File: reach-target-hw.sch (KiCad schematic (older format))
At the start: 29 parts, among them U1 nRF51822-QF, X1 16MHz 40ppm, X2 32.768kHz 20ppm

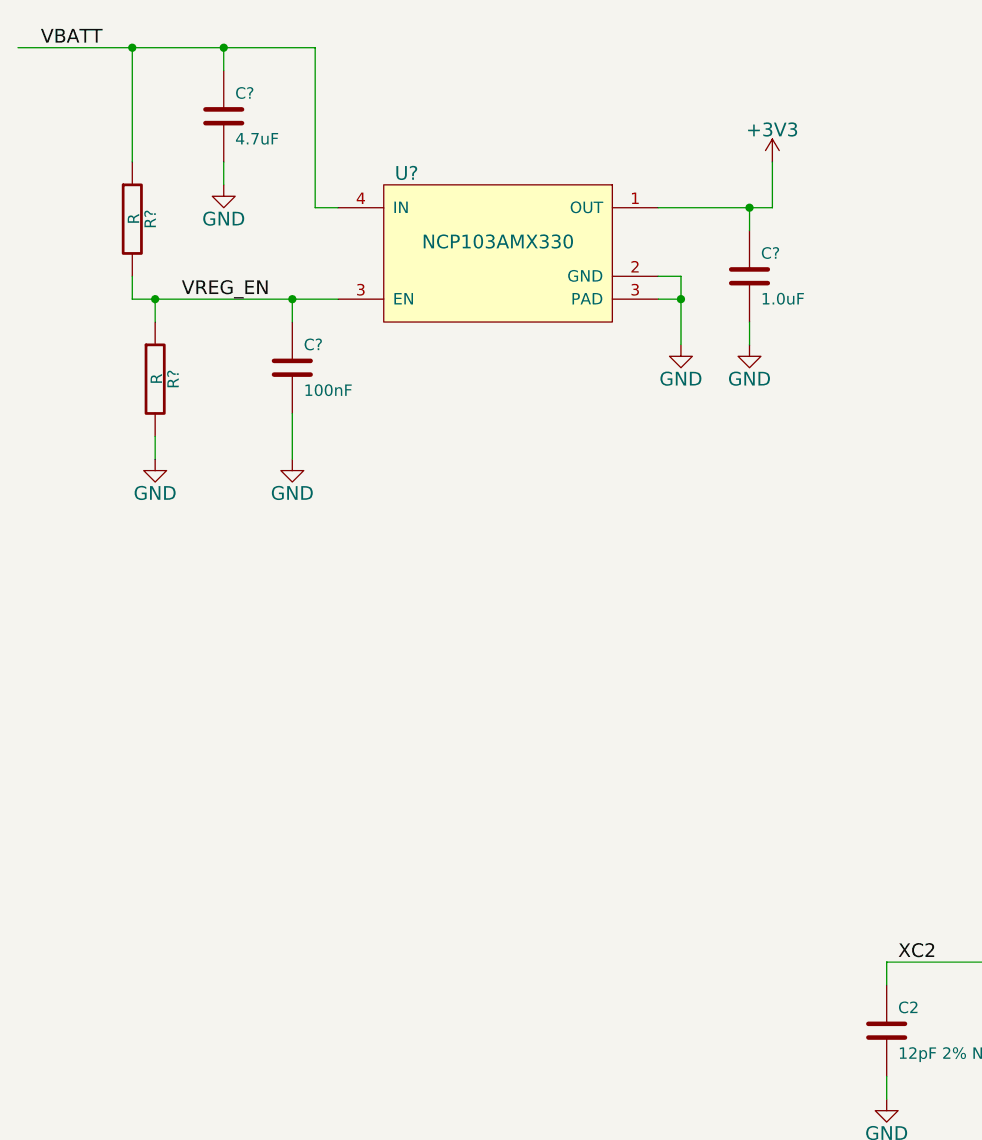
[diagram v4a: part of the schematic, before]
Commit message: added eeprom. can be no-popped
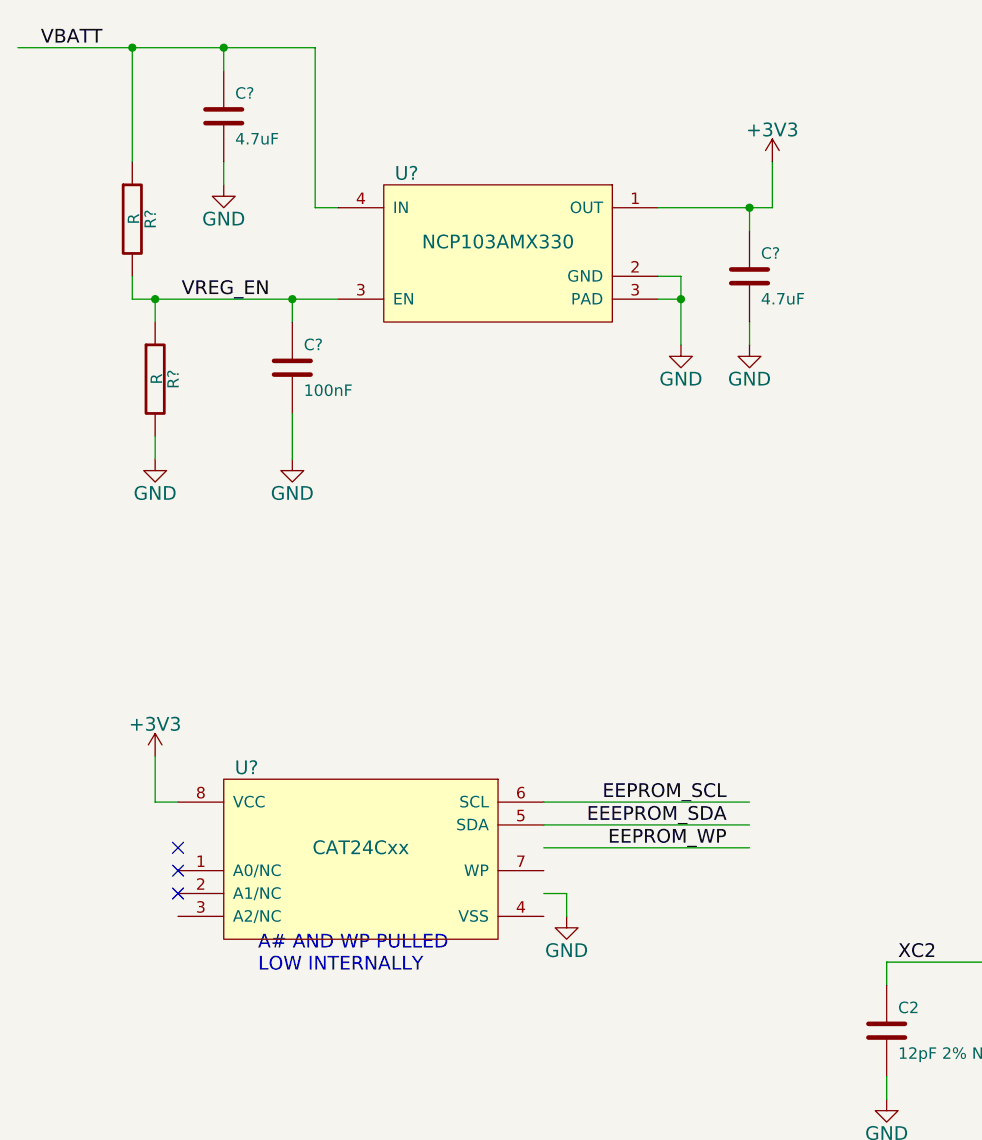
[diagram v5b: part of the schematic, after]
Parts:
- added U?: CAT24Cxx, symbol CAT24Cxx
- C?: value 1.0uF -> 4.7uF
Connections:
- net labels added: EEEPROM_SDA, EEPROM_SCL, EEPROM_WP
- wire segments 108 -> 115
- no-connect marks 1 -> 4
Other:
- note added: "A# AND WP PULLED\nLOW INTERNALLY"

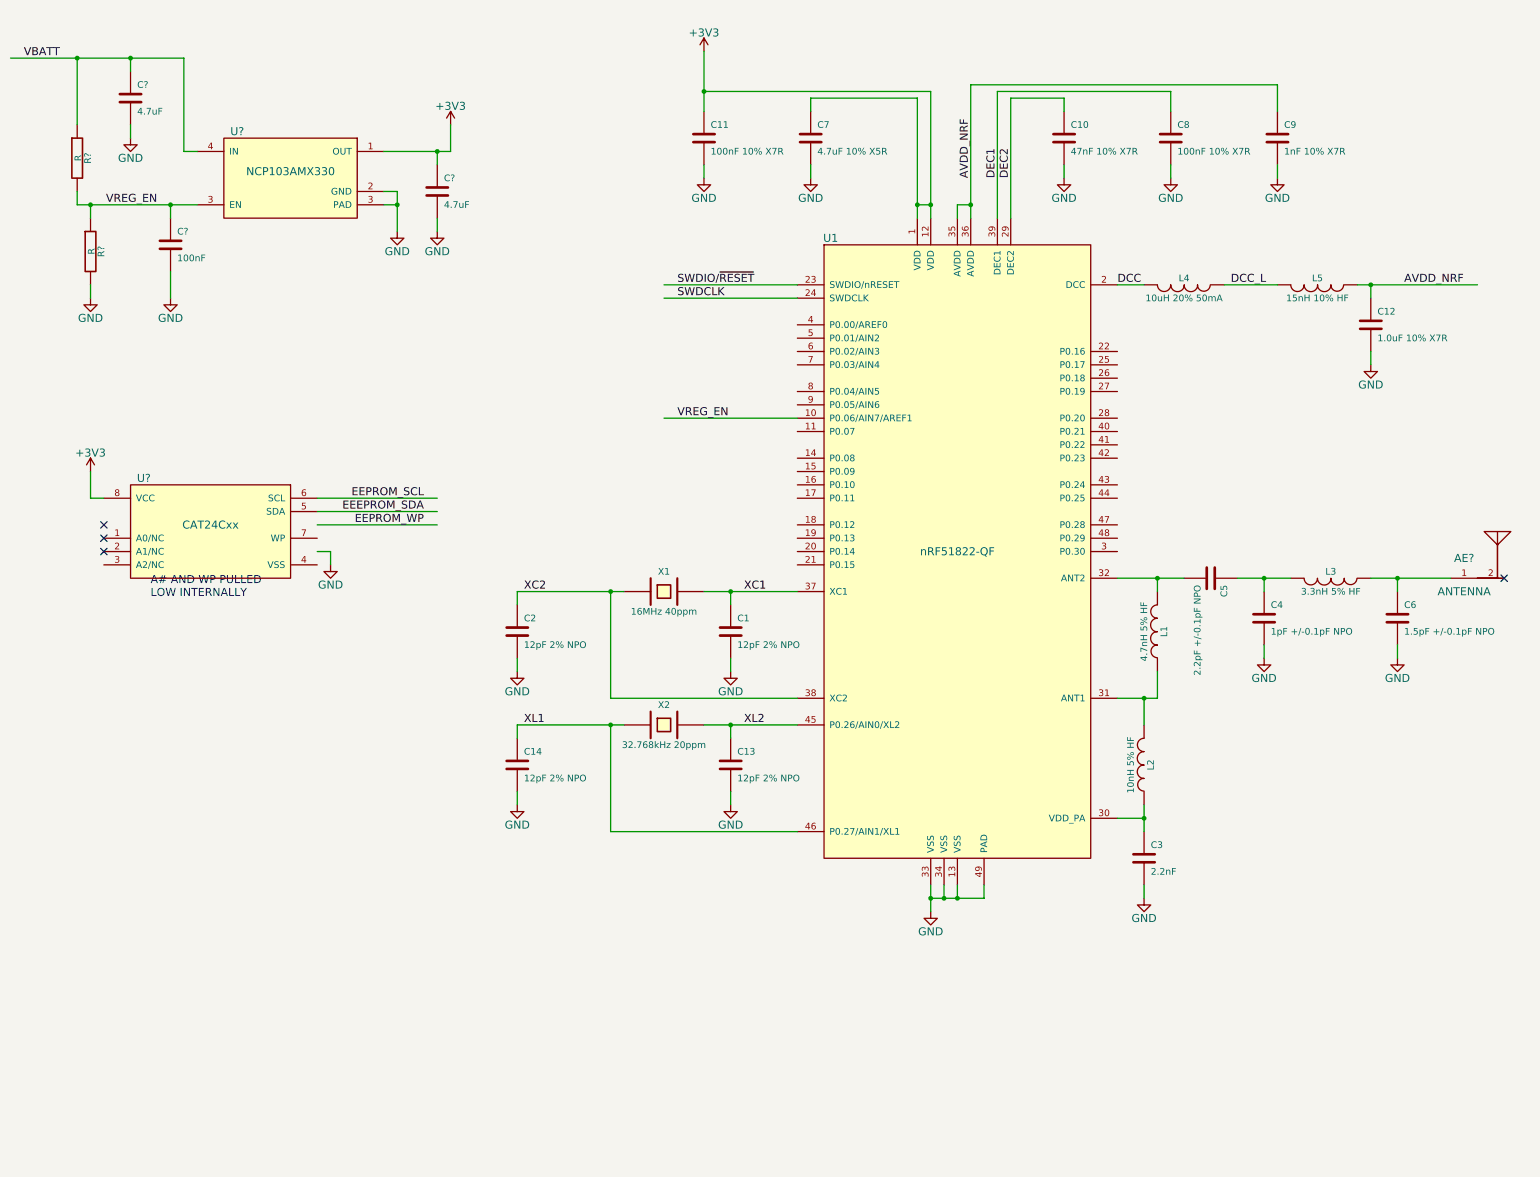
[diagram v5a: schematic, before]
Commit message: connected eeprom wp
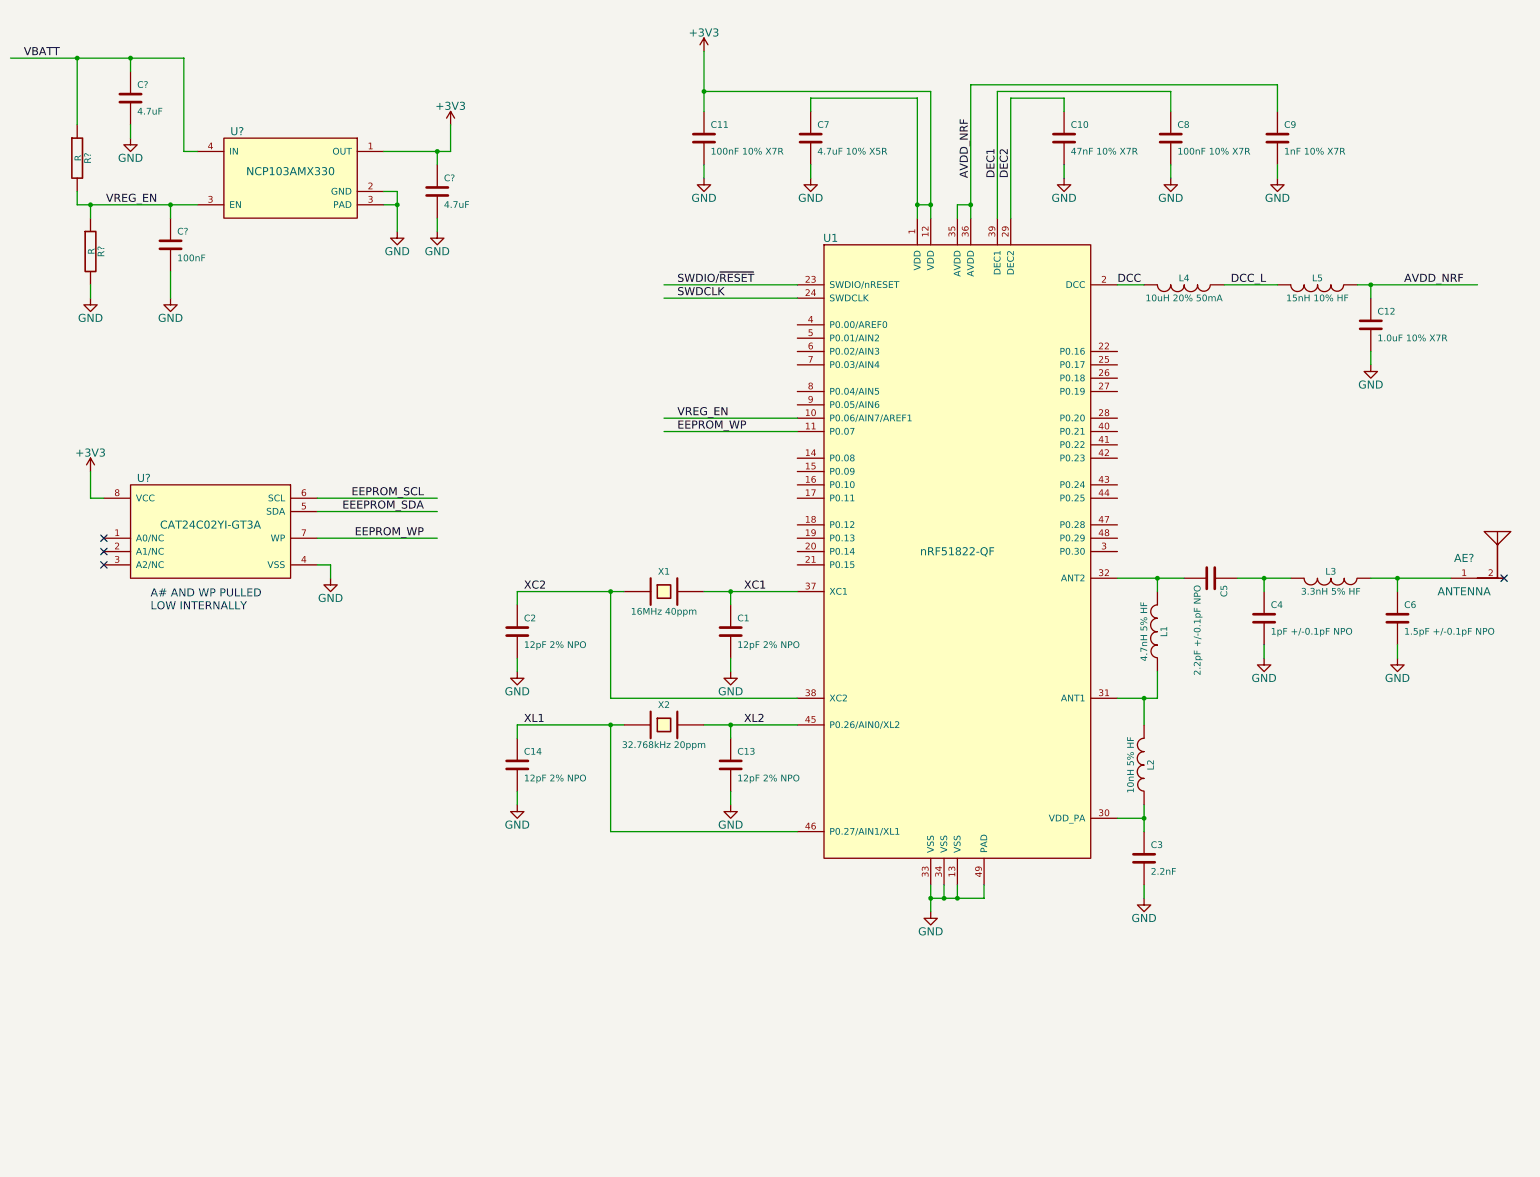
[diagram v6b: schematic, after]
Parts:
- U?: value CAT24Cxx -> CAT24C02YI-GT3A; footprint (none) -> Housings_SSOP:TSSOP-8_3x3mm_Pitch0.65mm
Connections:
- wire segments 115 -> 93
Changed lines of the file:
@@
 P 2800 5200
 F 0 "U?" H 2300 5550 60  0000 C CNN
-F 1 "CAT24Cxx" H 2800 5200 60  0000 C CNN
-F 2 "" H 2800 5200 60  0000 C CNN
-F 3 "" H 2800 5200 60  0000 C CNN
+F 1 "CAT24C02YI-GT3A" H 2800 5200 60  0000 C CNN
+F 2 "Housings_SSOP:TSSOP-8_3x3mm_Pitch0.65mm" H 2800 5200 60  0001 C CNN
+F 3 "http://www.onsemi.com/pub_link/Collateral/CAT24C01-D.PDF" H 2800 5200 60  0001 C CNN
 	1    2800 5200
 	1    0    0    -1
@@
 L GND #PWR?
 U 1 1 54D4057E
-P 3700 5500
-F 0 "#PWR?" H 3700 5250 60  0001 C CNN
-F 1 "GND" H 3700 5350 60  0000 C CNN
-F 2 "" H 3700 5500 60  0000 C CNN
-F 3 "" H 3700 5500 60  0000 C CNN
-	1    3700 5500
+P 3700 5600
+F 0 "#PWR?" H 3700 5350 60  0001 C CNN
+F 1 "GND" H 3700 5450 60  0000 C CNN
+F 2 "" H 3700 5600 60  0000 C CNN
+F 3 "" H 3700 5600 60  0000 C CNN
+	1    3700 5600
 	1    0    0    -1
 $EndComp
@@
 	1900 5000 1900 4800
 Wire Wire Line
-	3700 5400 3600 5400
-Wire Wire Line
-	3700 5500 3700 5400
+	3700 5500 3600 5500
+Wire Wire Line
+	3700 5600 3700 5500
 Wire Wire Line
 	6200 4400 7200 4400
@@
 Connection ~ 2500 2800
 Wire Wire Line
-	2500 2900 2500 2800
-Wire Wire Line
-	1800 2800 1900 2800
-Wire Wire Line
-	1900 2800 2500 2800
-Wire Wire Line
-	2500 2800 2700 2800
+	2500 2800 2500 2900
+Wire Wire Line
+	1800 2800 2700 2800
 Wire Wire Line
 	2200 2300 2200 2200
@@
 	2200 1700 2200 1800
 Wire Wire Line
-	1300 1700 1800 1700
-Wire Wire Line
-	1800 1700 2200 1700
-Wire Wire Line
-	2200 1700 2600 1700
+	1300 1700 2600 1700
 Wire Wire Line
 	2600 2400 2700 2400
@@
 	4200 2800 4100 2800
 Wire Wire Line
-	4200 2700 4200 2800
-Wire Wire Line
-	4200 2800 4200 3000
+	4200 2700 4200 3000
 Wire Wire Line
 	4100 2700 4200 2700
 Wire Wire Line
-	4100 2400 4500 2400
-Wire Wire Line
-	4500 2400 4600 2400
+	4100 2400 4600 2400
 Wire Wire Line
 	4600 2400 4600 2200
@@
 	11700 5600 11700 5700
 Wire Wire Line
-	11500 5600 11700 5600
-Wire Wire Line
-	11700 5600 12100 5600
+	11500 5600 12100 5600
 Connection ~ 10700 5600
 Wire Wire Line
@@
 	10700 5600 10700 5700
 Wire Wire Line
-	10500 5600 10700 5600
-Wire Wire Line
-	10700 5600 10900 5600
+	10500 5600 10900 5600
 Connection ~ 9900 5600
 Connection ~ 9800 7400
@@
 	9900 5600 9900 5700
 Wire Wire Line
-	9600 5600 9900 5600
-Wire Wire Line
-	9900 5600 10100 5600
-Wire Wire Line
-	9800 7300 9800 7400
-Wire Wire Line
-	9800 7400 9800 7500
+	9600 5600 10100 5600
+Wire Wire Line
+	9800 7300 9800 7500
 Wire Wire Line
 	9600 7400 9800 7400
@@
 	9900 6500 9900 6300
 Wire Wire Line
-	9600 6500 9800 6500
-Wire Wire Line
-	9800 6500 9900 6500
+	9600 6500 9900 6500
 Connection ~ 8500 2800
 Wire Wire Line
@@
 	8500 2800 8400 2800
 Wire Wire Line
-	8500 1900 8500 2800
-Wire Wire Line
-	8500 2800 8500 2900
+	8500 1900 8500 2900
 Wire Wire Line
 	10800 1900 10800 2100
@@
 	11500 3400 11500 3500
 Wire Wire Line
-	11400 3400 11500 3400
-Wire Wire Line
-	11500 3400 12300 3400
+	11400 3400 12300 3400
 Wire Wire Line
 	10400 3400 10800 3400
@@
 	5100 6700 5100 6800
 Wire Wire Line
-	5100 6700 5800 6700
-Wire Wire Line
-	5800 6700 5900 6700
+	5100 6700 5900 6700
 Wire Wire Line
 	5800 7500 5800 6700
@@
 	6700 7300 6700 7200
 Wire Wire Line
-	6500 6700 6700 6700
-Wire Wire Line
-	6700 6700 7200 6700
+	6500 6700 7200 6700
 Wire Wire Line
 	5100 6300 5100 6200
@@
 	5100 5700 5100 5800
 Wire Wire Line
-	5100 5700 5800 5700
-Wire Wire Line
-	5800 5700 5900 5700
+	5100 5700 5900 5700
 Wire Wire Line
 	5800 6500 5800 5700
@@
 	6700 6300 6700 6200
 Wire Wire Line
-	6500 5700 6700 5700
-Wire Wire Line
-	6700 5700 7200 5700
+	6500 5700 7200 5700
 Connection ~ 8100 2800
 Connection ~ 8200 2800
@@
 	8100 2800 8200 2800
 Wire Wire Line
-	8200 1950 8200 2800
-Wire Wire Line
-	8200 2800 8200 2900
+	8200 1950 8200 2900
 Wire Wire Line
 	6500 1950 8200 1950
 Wire Wire Line
-	6500 1650 6500 1950
-Wire Wire Line
-	6500 1950 6500 2100
+	6500 1650 6500 2100
 Wire Wire Line
 	6500 2600 6500 2500
@@
 	8100 2000 7300 2000
 Wire Wire Line
-	8100 2000 8100 2800
-Wire Wire Line
-	8100 2800 8100 2900
+	8100 2000 8100 2900
 Wire Wire Line
 	7300 2600 7300 2500
@@
 Connection ~ 8200 8000
 Wire Wire Line
-	8200 8000 8300 8000
-Wire Wire Line
-	8300 8000 8400 8000
-Wire Wire Line
-	8400 8000 8600 8000
+	8200 8000 8600 8000
 Wire Wire Line
 	8300 7900 8300 8000
 Wire Wire Line
-	8200 7900 8200 8000
-Wire Wire Line
-	8200 8000 8200 8100
-NoConn ~ 2000 5200
+	8200 7900 8200 8100
+NoConn ~ 2000 5500
 NoConn ~ 2000 5300
 NoConn ~ 2000 5400
@@
 Wire Wire Line
 	4500 5100 3600 5100
-Text Notes 2350 5750 0    60   ~ 0
+Text Notes 2350 5850 0    60   ~ 0
 A# AND WP PULLED\nLOW INTERNALLY
 Wire Wire Line
-	4500 5200 3600 5200
-Text Label 4400 5200 2    60   ~ 0
+	4500 5300 3600 5300
+Text Label 4400 5300 2    60   ~ 0
 EEPROM_WP
 Text Label 4400 5100 2    60   ~ 0
@@
 Text Label 4400 5000 2    60   ~ 0
 EEPROM_SCL
+Text Label 6300 4500 0    60   ~ 0
+EEPROM_WP
+Wire Wire Line
+	6200 4500 7200 4500
 $EndSCHEMATC

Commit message: labels
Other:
- note added: "3.3V LDO"
- note added: "I2C EEPROM"
- moved on the sheet: U?
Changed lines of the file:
@@
 L CAT24Cxx U?
 U 1 1 54D4022B
-P 2800 5200
-F 0 "U?" H 2300 5550 60  0000 C CNN
-F 1 "CAT24C02YI-GT3A" H 2800 5200 60  0000 C CNN
-F 2 "Housings_SSOP:TSSOP-8_3x3mm_Pitch0.65mm" H 2800 5200 60  0001 C CNN
-F 3 "http://www.onsemi.com/pub_link/Collateral/CAT24C01-D.PDF" H 2800 5200 60  0001 C CNN
-	1    2800 5200
+P 2400 5400
+F 0 "U?" H 1900 5750 60  0000 C CNN
+F 1 "CAT24C02YI-GT3A" H 2400 5400 60  0000 C CNN
+F 2 "Housings_SSOP:TSSOP-8_3x3mm_Pitch0.65mm" H 2400 5400 60  0001 C CNN
+F 3 "http://www.onsemi.com/pub_link/Collateral/CAT24C01-D.PDF" H 2400 5400 60  0001 C CNN
+	1    2400 5400
 	1    0    0    -1
 $EndComp
@@
 L GND #PWR?
 U 1 1 54D4057E
-P 3700 5600
-F 0 "#PWR?" H 3700 5350 60  0001 C CNN
-F 1 "GND" H 3700 5450 60  0000 C CNN
-F 2 "" H 3700 5600 60  0000 C CNN
-F 3 "" H 3700 5600 60  0000 C CNN
-	1    3700 5600
+P 3300 5800
+F 0 "#PWR?" H 3300 5550 60  0001 C CNN
+F 1 "GND" H 3300 5650 60  0000 C CNN
+F 2 "" H 3300 5800 60  0000 C CNN
+F 3 "" H 3300 5800 60  0000 C CNN
+	1    3300 5800
 	1    0    0    -1
 $EndComp
@@
 L +3V3 #PWR?
 U 1 1 54D4094C
-P 1900 4800
-F 0 "#PWR?" H 1900 4650 60  0001 C CNN
-F 1 "+3V3" H 1900 4940 60  0000 C CNN
-F 2 "" H 1900 4800 60  0000 C CNN
-F 3 "" H 1900 4800 60  0000 C CNN
-	1    1900 4800
+P 1500 5000
+F 0 "#PWR?" H 1500 4850 60  0001 C CNN
+F 1 "+3V3" H 1500 5140 60  0000 C CNN
+F 2 "" H 1500 5000 60  0000 C CNN
+F 3 "" H 1500 5000 60  0000 C CNN
+	1    1500 5000
 	1    0    0    -1
 $EndComp
 Wire Wire Line
-	2000 5000 1900 5000
-Wire Wire Line
-	1900 5000 1900 4800
-Wire Wire Line
-	3700 5500 3600 5500
-Wire Wire Line
-	3700 5600 3700 5500
+	1600 5200 1500 5200
+Wire Wire Line
+	1500 5200 1500 5000
+Wire Wire Line
+	3300 5700 3200 5700
+Wire Wire Line
+	3300 5800 3300 5700
 Wire Wire Line
 	6200 4400 7200 4400
@@
 Wire Wire Line
 	8200 7900 8200 8100
-NoConn ~ 2000 5500
-NoConn ~ 2000 5300
-NoConn ~ 2000 5400
-Wire Wire Line
-	4500 5000 3600 5000
-Wire Wire Line
-	4500 5100 3600 5100
-Text Notes 2350 5850 0    60   ~ 0
+NoConn ~ 1600 5700
+NoConn ~ 1600 5500
+NoConn ~ 1600 5600
+Wire Wire Line
+	4100 5200 3200 5200
+Wire Wire Line
+	4100 5300 3200 5300
+Text Notes 1950 6050 0    60   ~ 0
 A# AND WP PULLED\nLOW INTERNALLY
 Wire Wire Line
-	4500 5300 3600 5300
-Text Label 4400 5300 2    60   ~ 0
+	4100 5500 3200 5500
+Text Label 4000 5500 2    60   ~ 0
 EEPROM_WP
-Text Label 4400 5100 2    60   ~ 0
+Text Label 4000 5300 2    60   ~ 0
 EEEPROM_SDA
-Text Label 4400 5000 2    60   ~ 0
+Text Label 4000 5200 2    60   ~ 0
 EEPROM_SCL
 Text Label 6300 4500 0    60   ~ 0
@@
 Wire Wire Line
 	6200 4500 7200 4500
+Text Notes 3150 1450 0    60   ~ 0
+3.3V LDO
+Text Notes 2150 4600 0    60   ~ 0
+I2C EEPROM
 $EndSCHEMATC

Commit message: LEDs
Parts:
- added C?: 1nF, !Parts:SMD-0603, symbol C
- added D?: BLUE, symbol LED
- added D?: RED, symbol LED
- added R?: 100kR, symbol R
- added R? (x2): 1kR, symbol R
- added SW?: SW_PUSH, symbol SW_PUSH
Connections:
- net labels added: BLUE_LED, BUTTON, RED_LED
- wire segments 93 -> 136
